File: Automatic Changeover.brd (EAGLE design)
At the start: 174 x 152.1 mm, 49 parts, among them IC1 ACS750LCA-050, IC2 XMEGA16A4A, IC4 ACS750LCA-050, IC5 ACS750LCA-050, K1 S216SE1, K2 S216SE1, K3 S216SE1, K4 S216SE1, K5 S216SE1, K6 S216SE1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

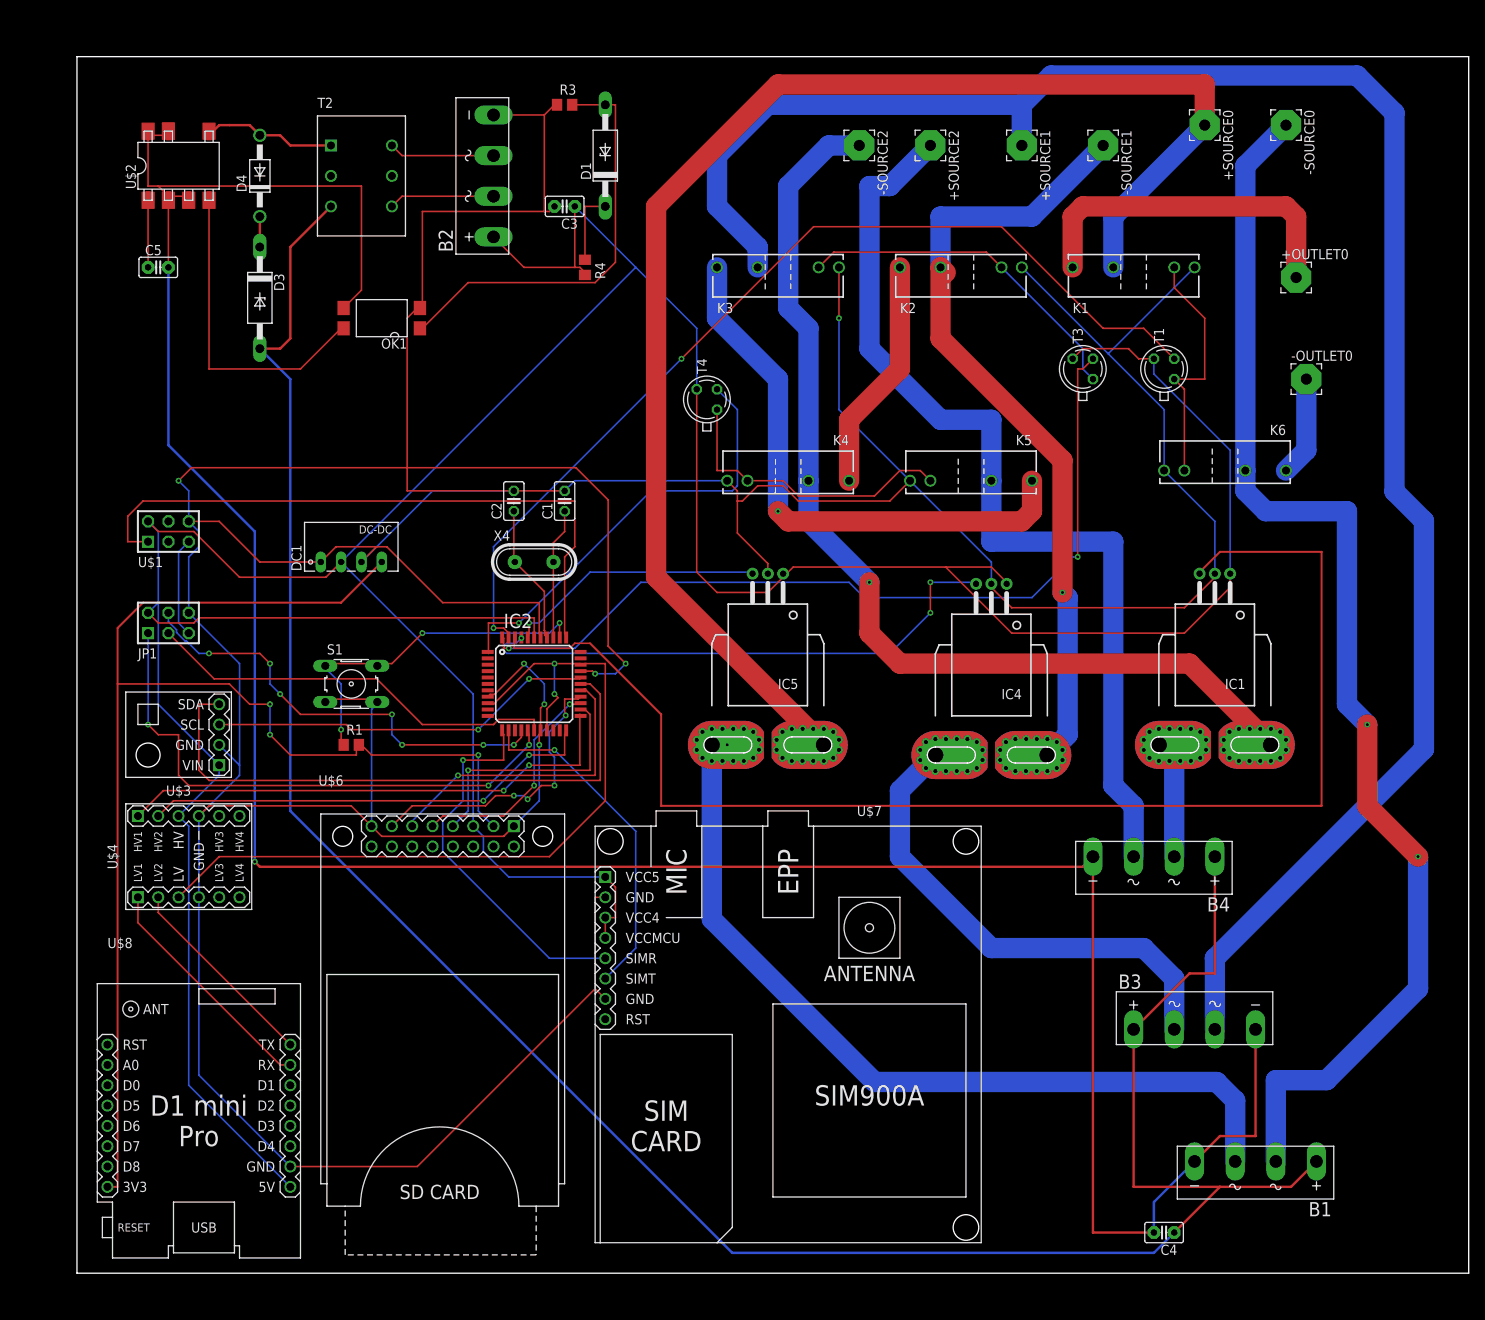
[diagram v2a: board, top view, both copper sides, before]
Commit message: added ground plane
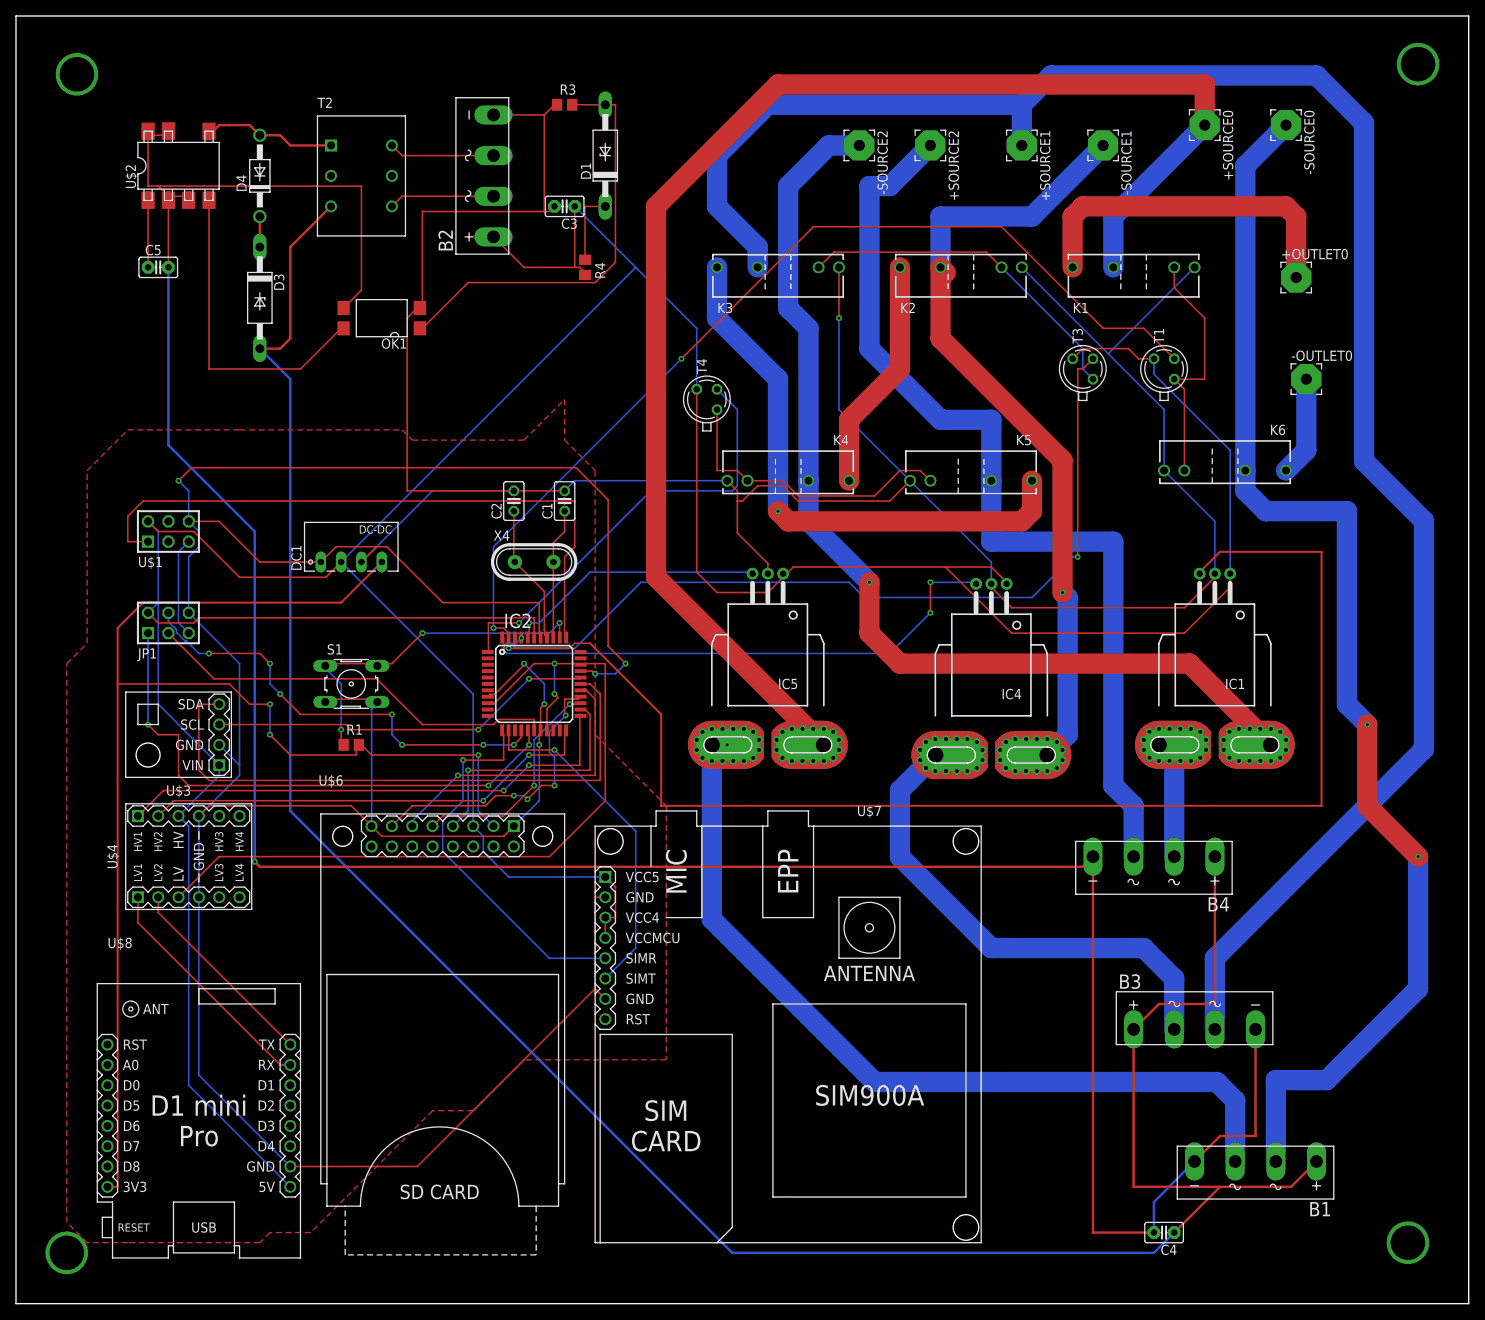
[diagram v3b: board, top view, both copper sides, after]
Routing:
- net +SOURCE1: track 238.8 -> 235.8 mm
- net N$17: track 296.3 -> 298.6 mm
- added copper zone on layer 1, net GND
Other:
- board size 174 x 152.1 mm -> 181.6 x 161 mm
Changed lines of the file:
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@@
 <drawing>
 <settings>
-<setting alwaysvectorfont="no"/>
+<setting alwaysvectorfont="yes"/>
 <setting verticaltext="up"/>
 </settings>
@@
 <layer number="43" name="vRestrict" color="2" fill="10" visible="yes" active="yes"/>
 <layer number="44" name="Drills" color="7" fill="1" visible="no" active="yes"/>
-<layer number="45" name="Holes" color="7" fill="1" visible="no" active="yes"/>
+<layer number="45" name="Holes" color="7" fill="1" visible="yes" active="yes"/>
 <layer number="46" name="Milling" color="3" fill="1" visible="no" active="yes"/>
 <layer number="47" name="Measures" color="7" fill="1" visible="no" active="yes"/>
@@
 <board>
 <plain>
-<wire x1="0" y1="0" x2="173.97" y2="0" width="0" layer="20"/>
-<wire x1="173.97" y1="0" x2="173.97" y2="152.07" width="0" layer="20"/>
-<wire x1="173.97" y1="152.07" x2="0" y2="152.07" width="0" layer="20"/>
-<wire x1="0" y1="152.07" x2="0" y2="0" width="0" layer="20"/>
+<wire x1="-7.62" y1="-3.81" x2="173.97" y2="-3.81" width="0" layer="20"/>
+<wire x1="173.97" y1="-3.81" x2="173.97" y2="157.15" width="0" layer="20"/>
+<wire x1="173.97" y1="157.15" x2="-7.62" y2="157.15" width="0" layer="20"/>
+<wire x1="-7.62" y1="157.15" x2="-7.62" y2="-3.81" width="0" layer="20"/>
 </plain>
 <attributes>
@@
 <wire x1="13.97" y1="97.79" x2="13.97" y2="93.98" width="0.2032" layer="16"/>
 <wire x1="62.3773" y1="100.6856" x2="14.3256" y2="100.6856" width="0.2032" layer="1"/>
+<polygon width="0.2032" layer="1">
+<vertex x="60.96" y="109.22"/>
+<vertex x="60.96" y="104.14"/>
+<vertex x="64.77" y="100.33"/>
+<vertex x="64.77" y="67.31"/>
+<vertex x="73.66" y="58.42"/>
+<vertex x="73.66" y="35.56"/>
+<vertex x="73.66" y="26.67"/>
+<vertex x="55.88" y="26.67"/>
+<vertex x="49.53" y="20.32"/>
+<vertex x="44.45" y="20.32"/>
+<vertex x="34.29" y="10.16"/>
+<vertex x="29.21" y="5.08"/>
+<vertex x="24.13" y="5.08"/>
+<vertex x="22.86" y="3.81"/>
+<vertex x="6.35" y="3.81"/>
+<vertex x="1.27" y="3.81"/>
+<vertex x="-1.27" y="6.35"/>
+<vertex x="-1.27" y="25.4"/>
+<vertex x="-1.27" y="76.2"/>
+<vertex x="1.27" y="78.74"/>
+<vertex x="1.27" y="100.33"/>
+<vertex x="6.35" y="105.41"/>
+<vertex x="20.32" y="105.41"/>
+<vertex x="40.64" y="105.41"/>
+<vertex x="41.91" y="104.14"/>
+<vertex x="55.88" y="104.14"/>
+</polygon>
 </signal>
 <signal name="XT2">
@@
 <wire x1="132.08" y1="10.795" x2="132.08" y2="30.48" width="0.3048" layer="1"/>
 <wire x1="142.875" y1="10.795" x2="132.08" y2="10.795" width="0.3048" layer="1"/>
-<wire x1="142.24" y1="37.465" x2="142.24" y2="52.07" width="0.3048" layer="1"/>
-<wire x1="139.065" y1="37.465" x2="142.24" y2="37.465" width="0.3048" layer="1"/>
-<wire x1="132.08" y1="30.48" x2="139.065" y2="37.465" width="0.3048" layer="1"/>
+<wire x1="142.24" y1="33.655" x2="142.24" y2="52.07" width="0.3048" layer="1"/>
+<wire x1="135.255" y1="33.655" x2="142.24" y2="33.655" width="0.3048" layer="1"/>
+<wire x1="132.08" y1="30.48" x2="135.255" y2="33.655" width="0.3048" layer="1"/>
 <wire x1="26.67" y1="111.76" x2="26.67" y2="57.785" width="0.3048" layer="16"/>
 <wire x1="26.67" y1="111.76" x2="22.86" y2="115.57" width="0.3048" layer="16"/>
@@
 <wire x1="85.09" y1="128.27" x2="80.01" y2="133.35" width="2.54" layer="16"/>
 <wire x1="85.09" y1="128.27" x2="85.09" y2="125.73" width="2.54" layer="16"/>
-<wire x1="164.6936" y1="145.0342" x2="160.02" y2="149.7078" width="2.54" layer="16"/>
-<wire x1="164.6936" y1="97.71903125" x2="164.6936" y2="145.0342" width="2.54" layer="16"/>
+<wire x1="160.8836" y1="143.7642" x2="154.94" y2="149.7078" width="2.54" layer="16"/>
+<wire x1="160.8836" y1="101.52903125" x2="160.8836" y2="143.7642" width="2.54" layer="16"/>
 <wire x1="142.24" y1="30.48" x2="142.24" y2="39.37" width="2.54" layer="16"/>
 <wire x1="168.3726" y1="65.5026" x2="142.24" y2="39.37" width="2.54" layer="16"/>
 <wire x1="168.3726" y1="65.5026" x2="168.3726" y2="94.04003125" width="2.54" layer="16"/>
-<wire x1="168.3726" y1="94.04003125" x2="164.6936" y2="97.71903125" width="2.54" layer="16"/>
-<wire x1="160.02" y1="149.7078" x2="121.7678" y2="149.7078" width="2.54" layer="16"/>
+<wire x1="168.3726" y1="94.04003125" x2="160.8836" y2="101.52903125" width="2.54" layer="16"/>
+<wire x1="154.94" y1="149.7078" x2="121.7678" y2="149.7078" width="2.54" layer="16"/>
 <wire x1="121.7678" y1="149.7078" x2="118.11" y2="146.05" width="2.54" layer="16"/>
 </signal>
@@
 <wire x1="7.62" y1="46.99" x2="7.62" y2="43.815" width="0.2032" layer="1"/>
 </signal>
+<signal name="N$1">
+<via x="167.64" y="151.13" extent="1-16" drill="4.318"/>
+</signal>
+<signal name="N$3">
+<via x="0" y="149.86" extent="1-16" drill="4.318"/>
+</signal>
+<signal name="N$4">
+<via x="-1.27" y="2.54" extent="1-16" drill="4.318"/>
+</signal>
+<signal name="N$5">
+<via x="166.37" y="3.81" extent="1-16" drill="4.318"/>
+</signal>
 </signals>
 <mfgpreviewcolors>
-<mfgpreviewcolor name="soldermaskcolor" color="0xC8008000"/>
+<mfgpreviewcolor name="soldermaskcolor" color="0xC8000000"/>
 <mfgpreviewcolor name="silkscreencolor" color="0xFFFEFEFE"/>
 <mfgpreviewcolor name="backgroundcolor" color="0xFF282828"/>
@@
 <mfgpreviewcolor name="substratecolor" color="0xFF786E46"/>
 </mfgpreviewcolors>
+<errors>
+</errors>
 </board>
 </drawing>

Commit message: Some few adjustments
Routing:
- net IN1: track 68.4 -> 74.7 mm
- net GND: track 713.7 -> 718.2 mm
- net +5V: track 498.1 -> 502.0 mm
- net OUT2: track 55.4 -> 58.3 mm
- net N$17: track 298.6 -> 300.1 mm
- net IN0: track 32.4 -> 33.9 mm
- net IN2: track 166.0 -> 167.5 mm
- net PDI_CLK: track 44.7 -> 45.7 mm
- net OUT0: track 121.4 -> 120.7 mm

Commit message: Perfecting the traces
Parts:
- moved U$2 6.35 mm to (6.35, 138.4)
- moved C5 5.08 mm to (5.08, 125.7)
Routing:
- net N$41: track 337.2 -> 359.2 mm
- net N$45: track 40.5 -> 55.0 mm
- net N$36: track 16.8 -> 23.2 mm
- net N$40: track 52.9 -> 58.5 mm
- net GND: track 718.2 -> 715.6 mm
- net +5V: track 502.0 -> 504.4 mm
- net N$14: track 16.9 -> 15.0 mm
- net -SOURCE1: track 99.9 -> 98.9 mm
- net N$44: track 8.89 -> 9.42 mm

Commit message: Fine tunning the board
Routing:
- net GND: track 715.6 -> 726.0 mm
- net +SOURCE1: track 235.8 -> 239.4 mm
- net N$41: track 359.2 -> 356.6 mm
- net N$63: track 37.4 -> 39.6 mm
- net +5V: track 504.4 -> 506.0 mm, vias 0 -> 1
- net N$39: track 9.21 -> 7.72 mm
- net OUT1: track 105.5 -> 106.6 mm
- net +OUTLET0: track 70.2 -> 71.3 mm
- net -SOURCE2: track 127.0 -> 126.0 mm
- net N$17: track 300.1 -> 300.8 mm
- net OUT2: track 58.3 -> 59.1 mm
- net IN2: track 167.5 -> 168.2 mm
- net -SOURCE1: track 98.9 -> 98.4 mm
- added copper zone on layer 16, net GND
